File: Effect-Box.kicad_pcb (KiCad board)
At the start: 6 copper layers, 170 parts, among them J1 Conn_02x07_Odd_Even, J10 Power pins, J2 26642801RP2, J3 FH12A-10S-0.5SH55, J5 Conn_ARM_JTAG_SWD_20, J6 26642801RP2, J7 AudioJack3, J8 AudioJack3, J9 PJ-006A-SMT, SW0 SW_Push, SW1 SW_Push, SW2 SW_Push, SW3 SW_Push, SW4 SW_Push, SW5 SW_Push, SW6 SW_Push, U1 TPS54325, U10 LM7805SX_NOPB, U2 TPS54294, U3 XC7A100T-FTG256, U4 S25FL1, U5 SiT2024B, U6 AS6C1616, U7 EFM32GG942F1024, U8 INA1651IPW, U9 PCM3003E

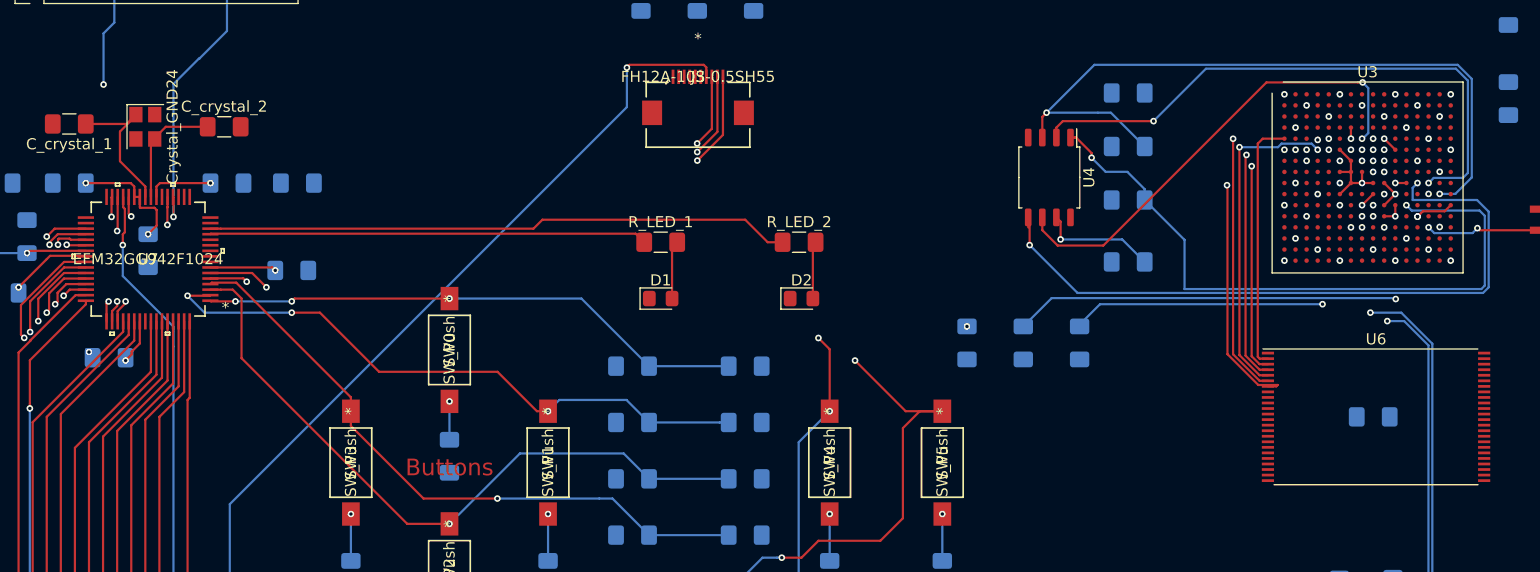
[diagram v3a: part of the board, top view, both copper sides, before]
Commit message: Route MCU to FPGA
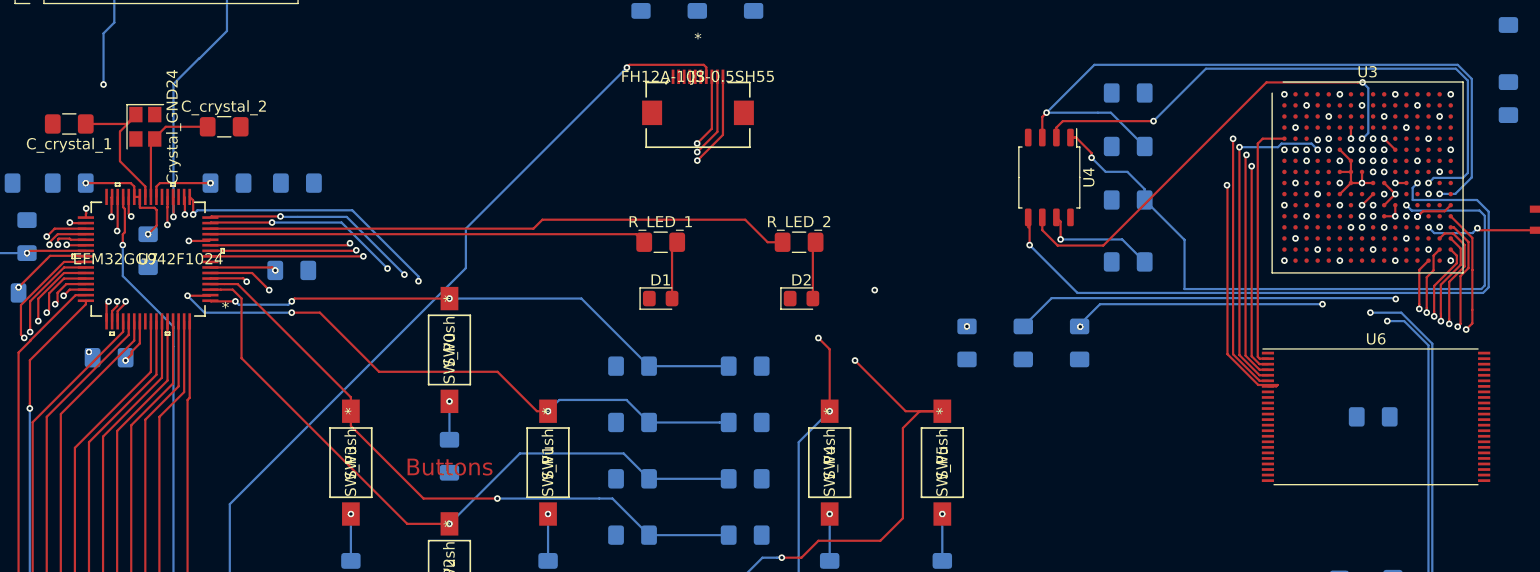
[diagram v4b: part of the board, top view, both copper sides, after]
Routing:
- net /FPGA/GPIO_3: track 0.00 -> 138.7 mm, vias 0 -> 3
- net /FPGA/GPIO_2: track 0.00 -> 134.6 mm, vias 0 -> 3
- net /FPGA/GPIO_1: track 0.00 -> 128.8 mm, vias 0 -> 3
- net /FPGA/SS: track 0.00 -> 128.3 mm, vias 0 -> 2
- net /FPGA/GPIO_0: track 0.00 -> 127.9 mm, vias 0 -> 3
- net /FPGA/MOSI: track 0.00 -> 121.5 mm, vias 0 -> 2
- net /FPGA/MISO: track 0.00 -> 120.0 mm, vias 0 -> 2
- net /FPGA/SCLK: track 0.00 -> 118.0 mm, vias 0 -> 2
- net /FPGA/PROGRAM_B: track 36.6 -> 135.0 mm, vias 2 -> 4
- net /FPGA/DONE: track 70.4 -> 157.2 mm, vias 2 -> 3
- net Net-(C_reset1-Pad1): track 110.6 -> 93.9 mm

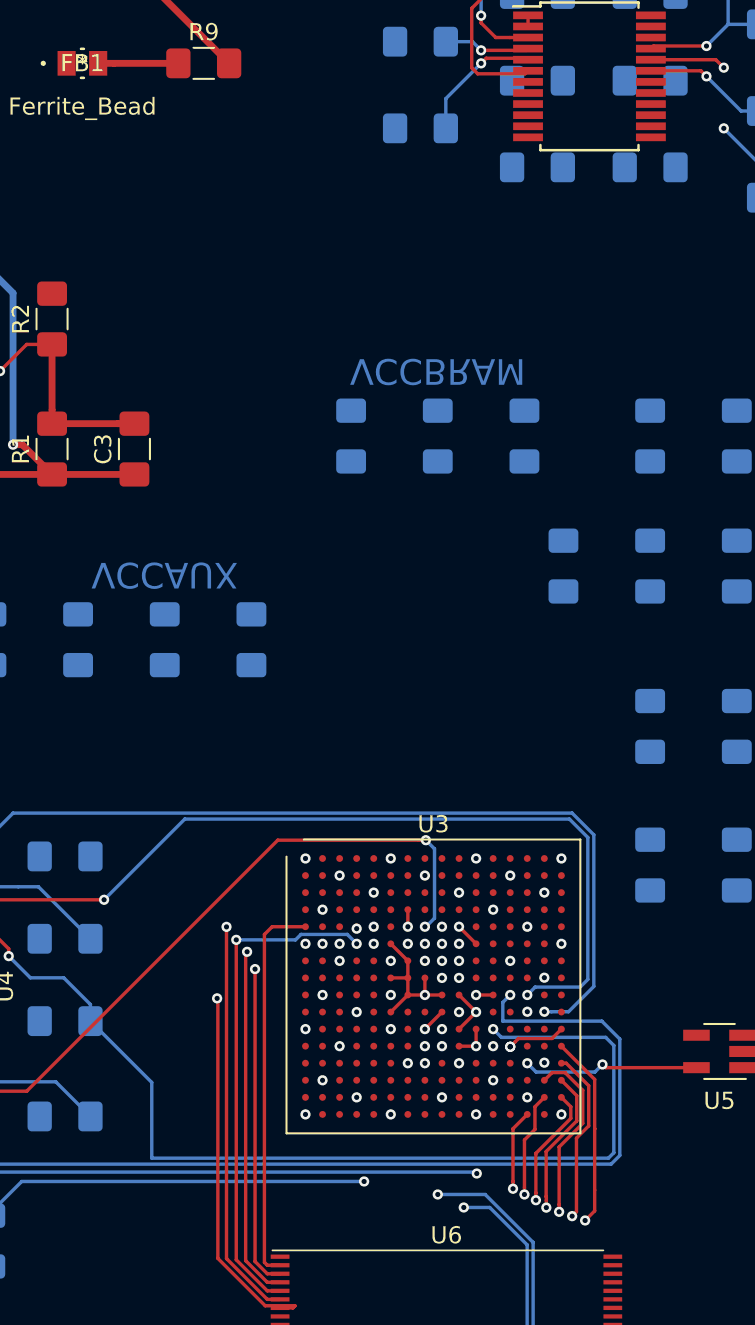
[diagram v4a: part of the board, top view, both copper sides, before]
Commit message: Route FPGA to DAC/ADC
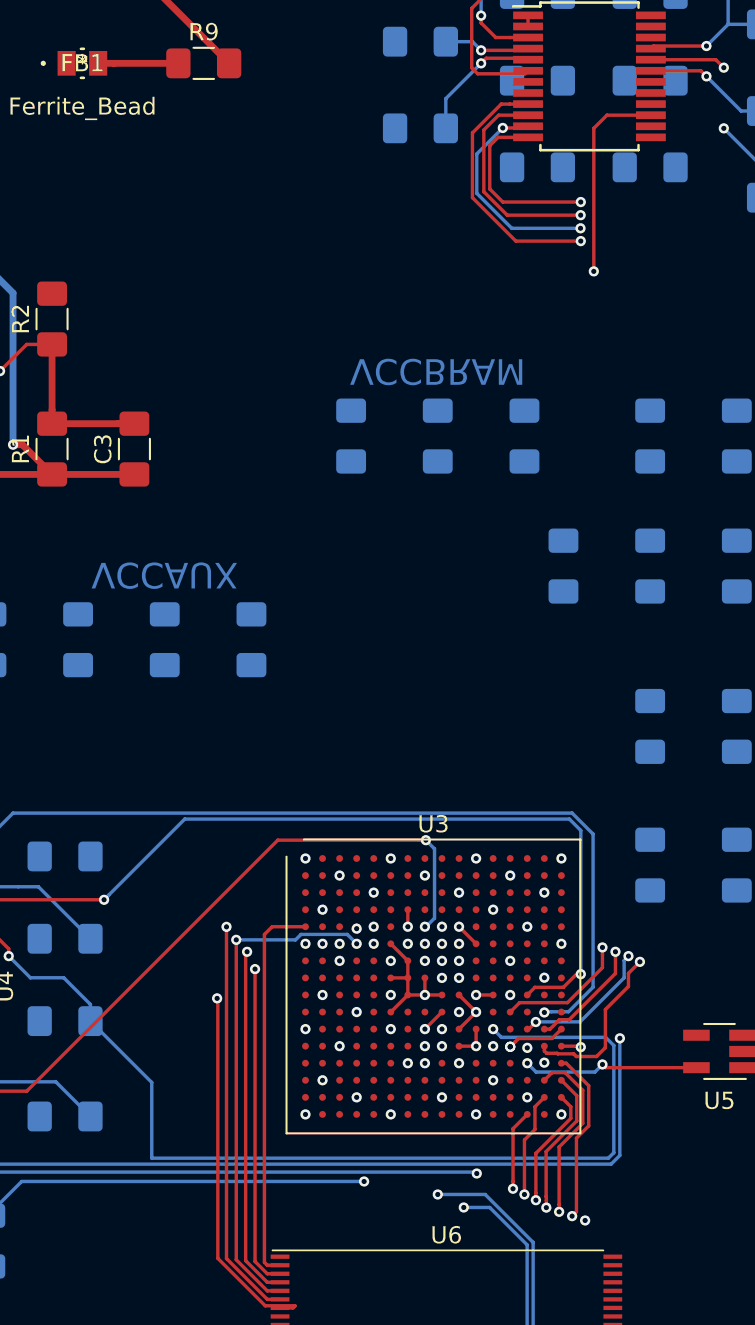
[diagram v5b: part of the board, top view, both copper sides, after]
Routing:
- net /FPGA/Audio I/O/LRCLK: track 0.00 -> 68.1 mm, vias 0 -> 2
- net /FPGA/Audio I/O/FPGAIn: track 0.00 -> 68.1 mm, vias 0 -> 2
- net /FPGA/Audio I/O/BITCLK: track 0.00 -> 65.1 mm, vias 0 -> 4
- net /FPGA/Audio I/O/SYSCLK: track 0.00 -> 64.4 mm, vias 0 -> 2
- net /FPGA/Audio I/O/FPGAOut: track 0.00 -> 59.6 mm, vias 0 -> 2
- net Net-(U3-PadJ14): track 52.9 -> 52.1 mm
- net /FPGA/DONE: track 157.2 -> 156.6 mm
- net /FPGA/GPIO_2: track 134.6 -> 134.8 mm, vias 3 -> 4
- net Net-(U3-PadJ13): track 62.7 -> 62.6 mm, vias 2 -> 3
- net GND: vias 37 -> 36

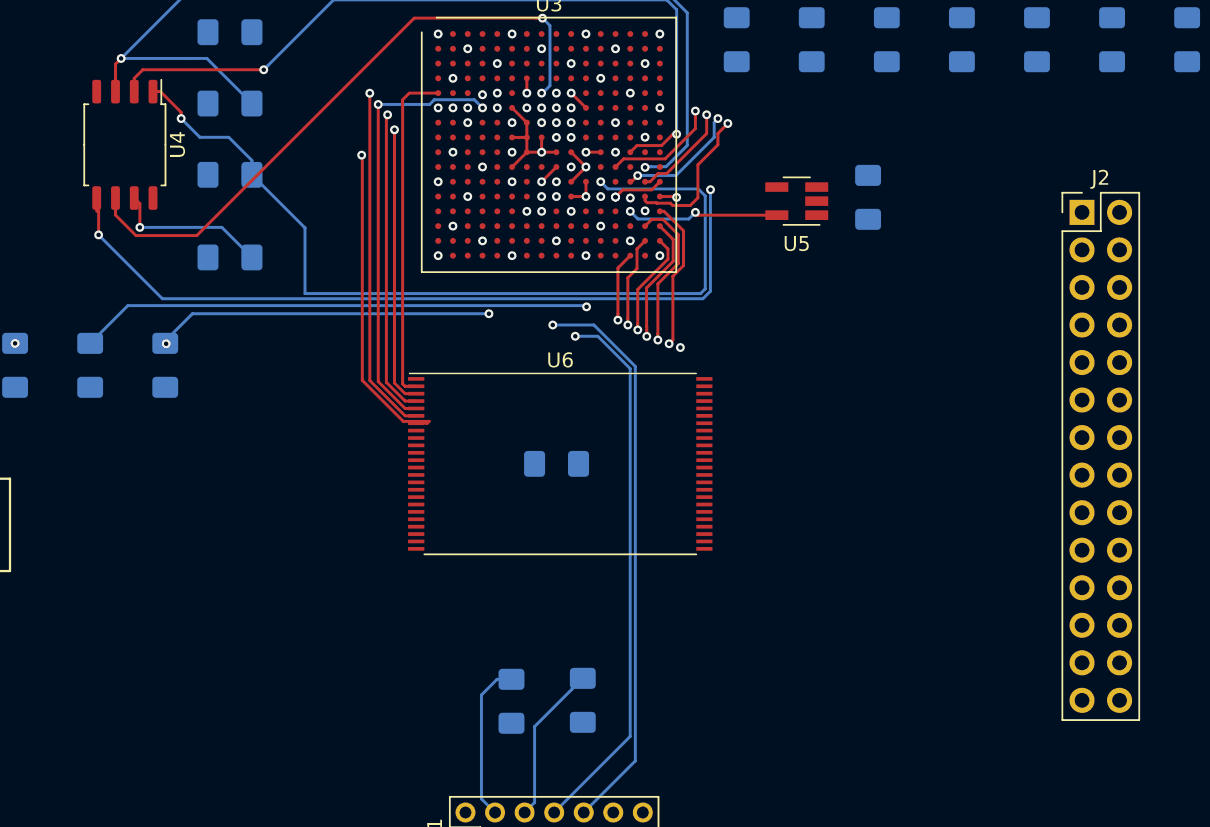
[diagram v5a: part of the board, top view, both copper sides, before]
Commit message: Partially route FPGA pinout
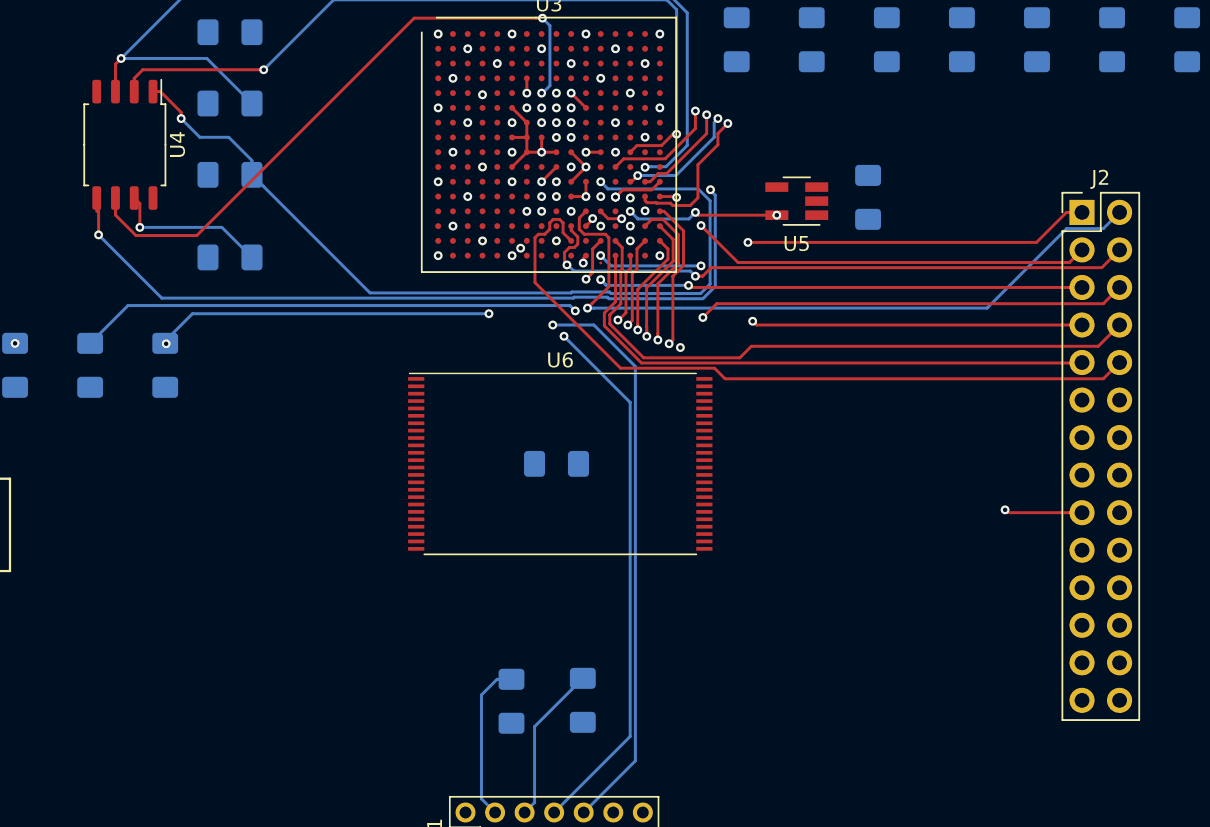
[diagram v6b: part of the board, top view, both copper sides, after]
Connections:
- J2 pad 17: /FPGA/FPGA_pinout_17 -> /FPGA/FPGA_pinout_clk
- J2 pad 18: /FPGA/FPGA_pinout_18 -> Net-(J2-Pad18)
- J2 pad 19: /FPGA/FPGA_pinout_19 -> Net-(J2-Pad19)
- J2 pad 20: /FPGA/FPGA_pinout_20 -> Net-(J2-Pad20)
- J2 pad 21: /FPGA/FPGA_pinout_21 -> Net-(J2-Pad21)
- J2 pad 22: /FPGA/FPGA_pinout_22 -> Net-(J2-Pad22)
- J2 pad 23: /FPGA/FPGA_pinout_23 -> Net-(J2-Pad23)
- J2 pad 24: /FPGA/FPGA_pinout_24 -> Net-(J2-Pad24)
- J2 pad 25: /FPGA/FPGA_pinout_25 -> Net-(J2-Pad25)
- J2 pad 26: /FPGA/FPGA_pinout_26 -> Net-(J2-Pad26)
- U3 pad N14: Net-(U3-PadN14) -> /FPGA/FPGA_pinout_clk
- U3 pad P6: /FPGA/FPGA_pinout_26 -> Net-(U3-PadP6)
- U3 pad R5: /FPGA/FPGA_pinout_22 -> Net-(U3-PadR5)
- U3 pad R6: /FPGA/FPGA_pinout_24 -> Net-(U3-PadR6)
- U3 pad R7: /FPGA/FPGA_pinout_25 -> Net-(U3-PadR7)
- U3 pad R8: /FPGA/FPGA_pinout_17 -> Net-(U3-PadR8)
- U3 pad T10: /FPGA/FPGA_pinout_21 -> Net-(U3-PadT10)
- U3 pad T5: /FPGA/FPGA_pinout_23 -> Net-(U3-PadT5)
- U3 pad T7: /FPGA/FPGA_pinout_18 -> Net-(U3-PadT7)
- U3 pad T8: /FPGA/FPGA_pinout_19 -> Net-(U3-PadT8)
- U3 pad T9: /FPGA/FPGA_pinout_20 -> Net-(U3-PadT9)
- U5 pad 5: Net-(U3-PadN14) -> /FPGA/FPGA_pinout_clk
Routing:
- net /FPGA/FPGA_pinout_10: track 0.00 -> 50.0 mm
- net /FPGA/FPGA_pinout_2: track 0.00 -> 47.7 mm, vias 0 -> 1
- net /FPGA/FPGA_pinout_8: track 0.00 -> 42.5 mm
- net /FPGA/FPGA_pinout_clk: track 0.00 -> 42.0 mm, vias 0 -> 4
- net /FPGA/FPGA_pinout_4: track 0.00 -> 41.9 mm, vias 0 -> 2
- net /FPGA/FPGA_pinout_6: track 0.00 -> 41.0 mm, vias 0 -> 2
- net /FPGA/FPGA_pinout_9: track 0.00 -> 38.4 mm
- net /FPGA/FPGA_pinout_5: track 0.00 -> 37.9 mm, vias 0 -> 3
- net /FPGA/FPGA_pinout_3: track 0.00 -> 36.7 mm, vias 0 -> 2
- net /FPGA/FPGA_pinout_7: track 0.00 -> 34.7 mm, vias 0 -> 4
- net /FPGA/SRAM_a10: track 32.6 -> 0.00 mm, vias 2 -> 0
- net /FPGA/SRAM_a9: track 32.4 -> 0.00 mm, vias 2 -> 0
- net /FPGA/FPGA_pinout_1: track 0.00 -> 31.9 mm, vias 0 -> 2
- net /FPGA/SRAM_a11: track 29.5 -> 0.00 mm, vias 2 -> 0
- net /FPGA/SRAM_a12: track 26.8 -> 0.00 mm, vias 2 -> 0
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
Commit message: Minor fixes
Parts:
- moved C35 13.8 mm to (199.4, 86.4)
- moved C49 13.8 mm to (258.3, 82.0)
- moved C51 13.8 mm to (253.2, 82.0)
- moved J6 13.8 mm to (136.7, 148.8)
- moved R_btn_up_2 13.8 mm to (169.2, 133.9)
- moved R_btn_up_4 13.8 mm to (169.2, 144.0)
- moved R_btn_up_5 13.8 mm to (169.2, 149.1)
- moved R_disp1 13.8 mm to (169.9, 90.2)
- moved SW1 13.8 mm to (151.4, 127.8)
- moved SW5 13.8 mm to (186.9, 127.8)
- moved J7 13.8 mm to (262.1, 39.6)
- moved J9 13.8 mm to (183.1, 37.1)
- moved R19 13.8 mm to (256.0, 27.9)
- moved C11 13.8 mm to (186.2, 67.1)
- moved C14 13.8 mm to (186.2, 60.5)
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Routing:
- net PWR_IN: track 155.6 -> 153.7 mm
- net GND: track 35.3 -> 33.5 mm
- net +5VA: track 68.5 -> 67.0 mm
- net /FPGA/FPGA_pinout_5: track 37.9 -> 36.9 mm
- net /FPGA/FPGA_pinout_6: track 41.0 -> 41.8 mm
- net +3V3: track 42.7 -> 42.1 mm, vias 19 -> 18
- net /FPGA/FPGA_pinout_7: vias 4 -> 3
